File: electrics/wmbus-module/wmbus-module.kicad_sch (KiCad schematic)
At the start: 23 parts, among them J1 North, J2 South, J3 West, J4 East, U1 BA033CC0FP-E2, U2 MAX3486

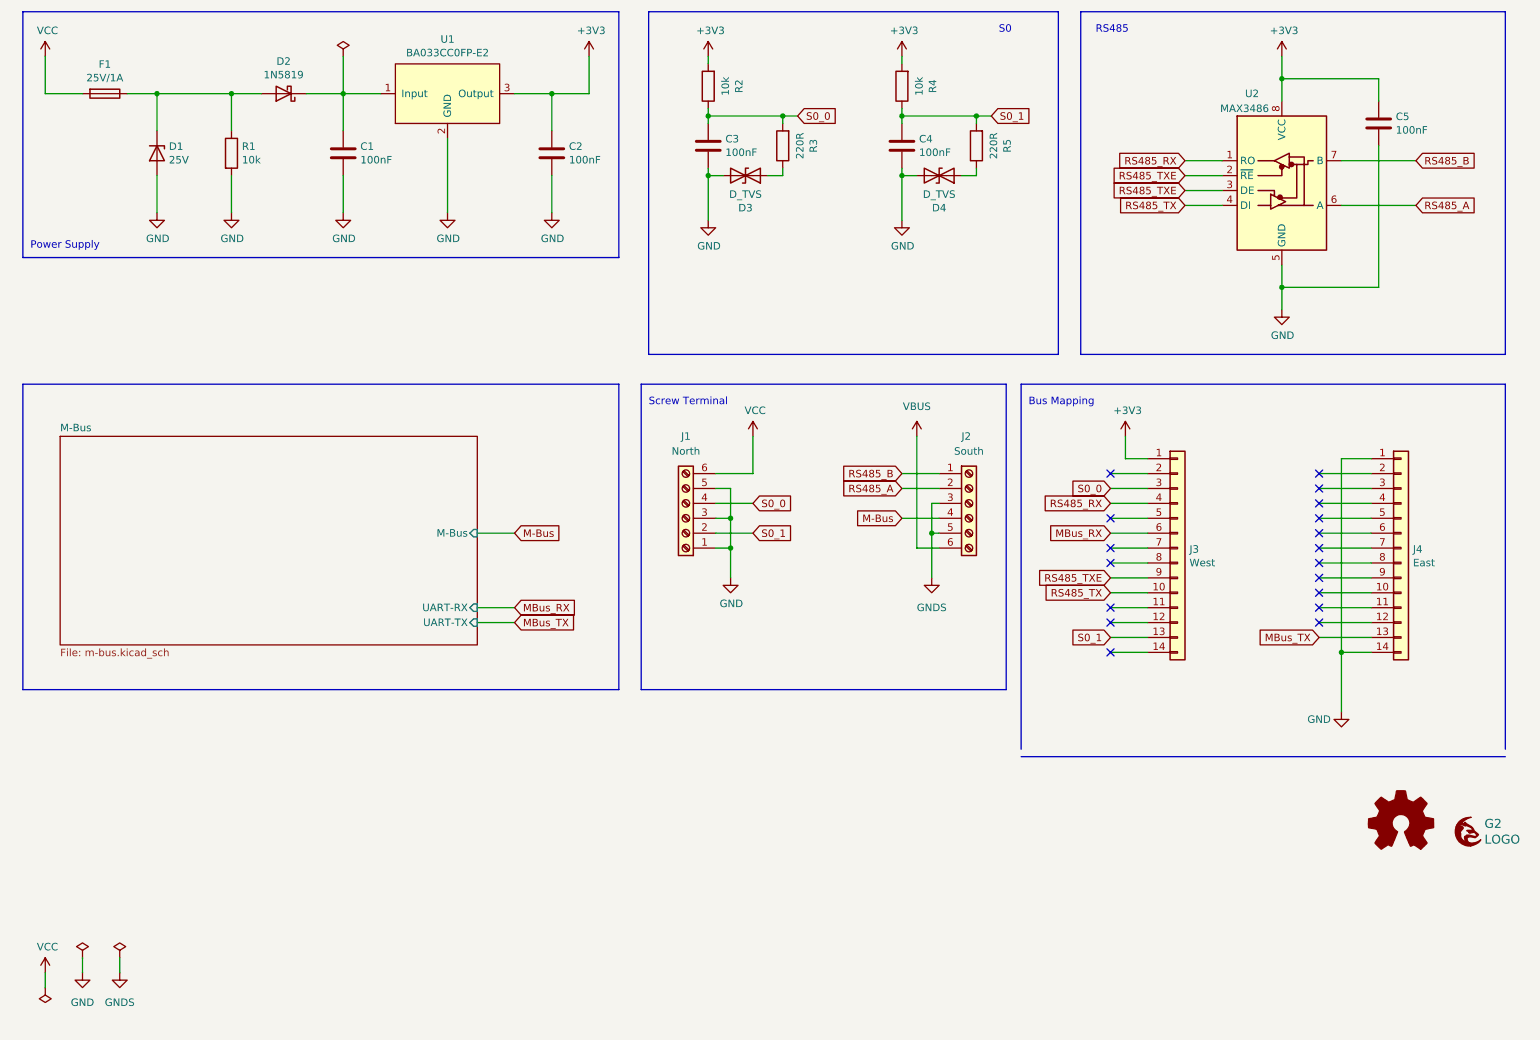
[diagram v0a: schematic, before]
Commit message: Fix all ERC and DRC warnings during build
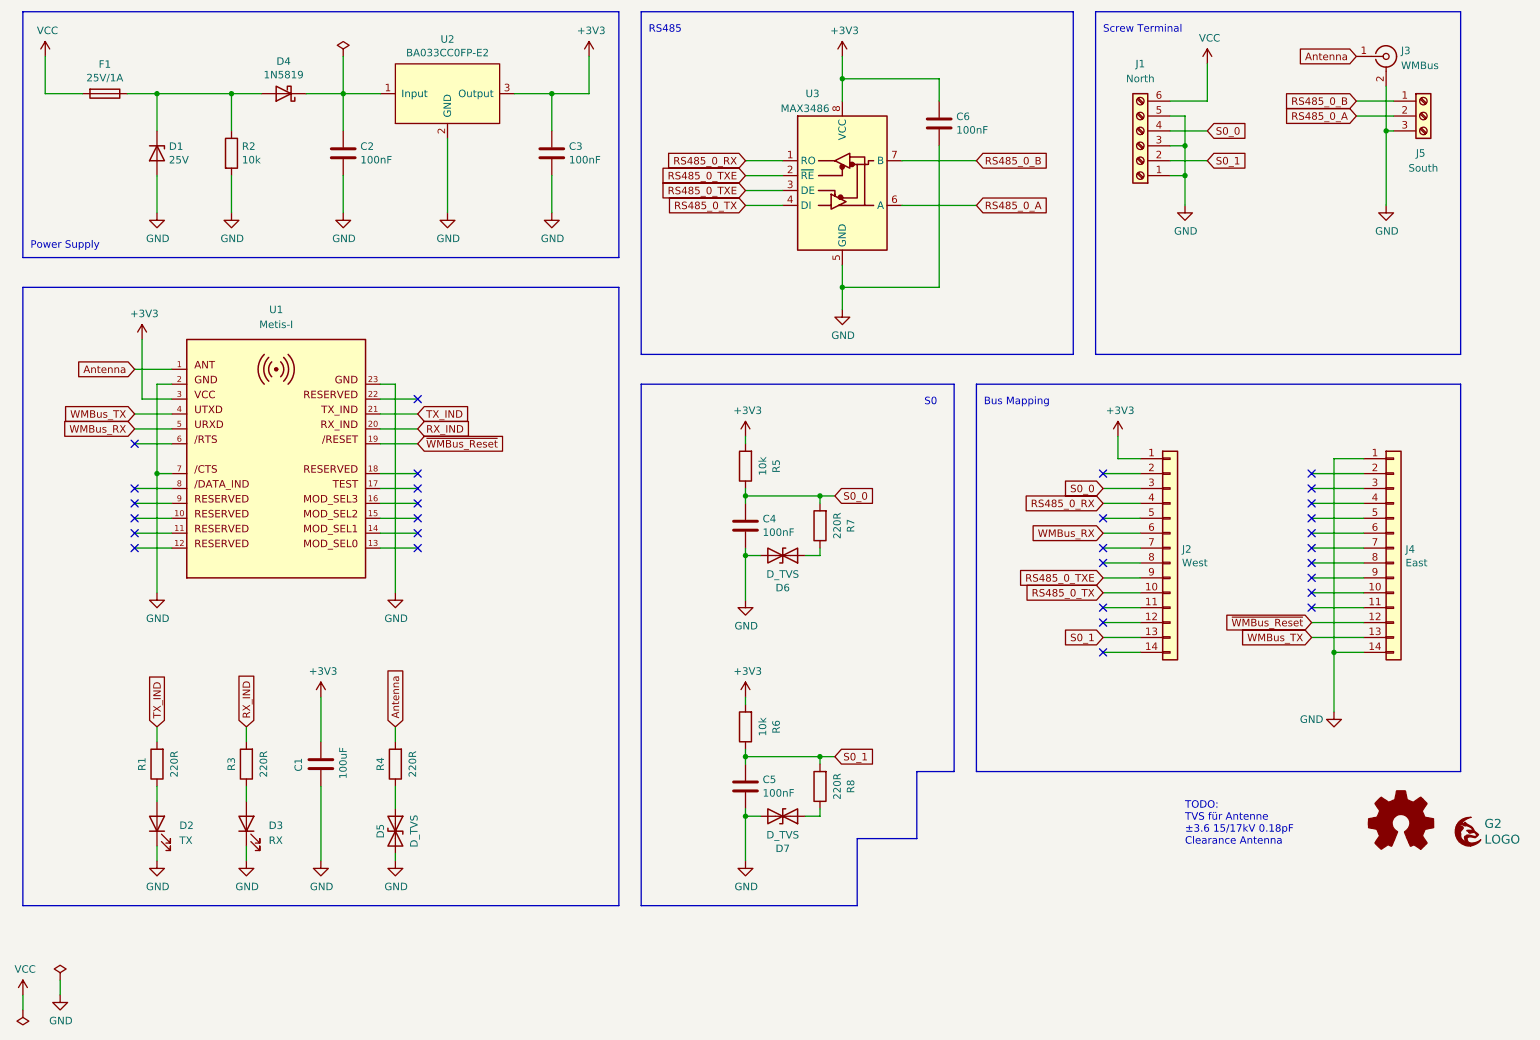
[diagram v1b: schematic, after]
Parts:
- removed C5: 100nF, Capacitor_SMD:C_0603_1608Metric_Pad1.08x0.95mm_HandSolder, symbol Device:C
- removed J2: South, footprints:PHOENIX_1935200, symbol Connector:Screw_Terminal_01x06
- added C1: 100uF, Capacitor_SMD:C_1206_3216Metric_Pad1.33x1.80mm_HandSolder, symbol Device:C
- added C6: 100nF, Capacitor_SMD:C_1206_3216Metric_Pad1.33x1.80mm_HandSolder, symbol Device:C
- added D2: TX, LED_SMD:LED_1206_3216Metric_Pad1.42x1.75mm_HandSolder, symbol Device:LED
- added D3: RX, LED_SMD:LED_1206_3216Metric_Pad1.42x1.75mm_HandSolder, symbol Device:LED
- added D5: D_TVS, Diode_SMD:D_0603_1608Metric_Pad1.05x0.95mm_HandSolder, symbol Device:D_TVS
- added J3: WMBus, Connector_Coaxial:SMA_Amphenol_901-143_Horizontal, symbol Connector:Conn_Coaxial
- added J5: South, footprints:PHOENIX_1711039, symbol Connector:Screw_Terminal_01x03
- added R1, R3, R4: 220R, Resistor_SMD:R_1206_3216Metric_Pad1.30x1.75mm_HandSolder, symbol Device:R
- added U1: Metis-I, footprints:WE-FP-1, symbol WIRL-WMB1_2607011113000:WIRL-WMB1_2607011113000
- C2: renamed from C1; Price (none) -> 0.24
- C3: renamed from C2; Price (none) -> 0.24
- C4: renamed from C3; Price (none) -> 0.24
- C5: renamed from C4; Price (none) -> 0.24
- D1: Price (none) -> 0.40
- D4: renamed from D2; Price (none) -> 0.25
- D6: renamed from D3; Price (none) -> 0.32
- D7: renamed from D4; Price (none) -> 0.32
- F1: Price (none) -> 0.93
- J2: renamed from J3; Price (none) -> 0.45
- J4: Price (none) -> 0.45
- R2: renamed from R1; Price (none) -> 0.08
- R5: renamed from R2; Price (none) -> 0.08
- R6: renamed from R4; Price (none) -> 0.08
- R7: renamed from R3; Price (none) -> 0.08
- R8: renamed from R5; Price (none) -> 0.08
- U2: renamed from U1; Price (none) -> 0.97
- U3: renamed from U2; Price (none) -> 3.71
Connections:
- net +3V3: now also C1.1, C6.1, U1.3
- net GND: now also C1.2, C6.2, D2.1 (K), D3.1 (K), D5.2 (A2), J3.2 (Ext), J5.3 (Pin_3), U1.2, U1.23, U1.7
- net ~{WMBus_Reset}: now reaches J4.12 (Pin_12)
- net ~{WMBus_Reset}: now also U1.19
- net MBus_RX renamed WMBus_RX
- net WMBus_RX: now also U1.5
- net MBus_TX renamed WMBus_TX
- net WMBus_TX: now also U1.4
- net RS485_A renamed RS485_0_A
- net RS485_0_A: now also J5.2 (Pin_2)
- net RS485_B renamed RS485_0_B
- net RS485_0_B: now also J5.1 (Pin_1)
- net RS485_RX renamed RS485_0_RX
- net RS485_TX renamed RS485_0_TX
- net RS485_TXE renamed RS485_0_TXE
- new net: D2.2 (A), R1.1
- new net: D5.1 (A1), R4.1
- new net: D3.2 (A), R3.1
- new net Antenna: J3.1 (In), R4.2, U1.1
- new net RX_IND: R3.2, U1.20
- new net TX_IND: R1.2, U1.21
- no-connect marks 18 -> 30
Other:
- removed sheet M-Bus
- note added: "TODO: TVS für Antenne ±3.6 15/17kV 0.18pF Clearance Antenna"
- title: M-Bus Metering Module -> Inoa Satellite WMBus Module
- moved on the sheet: C4, C5, D6, D7, J2, J4, R5, R6, R7, R8, U3
